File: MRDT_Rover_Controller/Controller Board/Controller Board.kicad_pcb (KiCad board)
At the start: 2 copper layers, 137.6 x 81.5 mm, 29 parts, among them Q1 S8050, U1 MCP3008

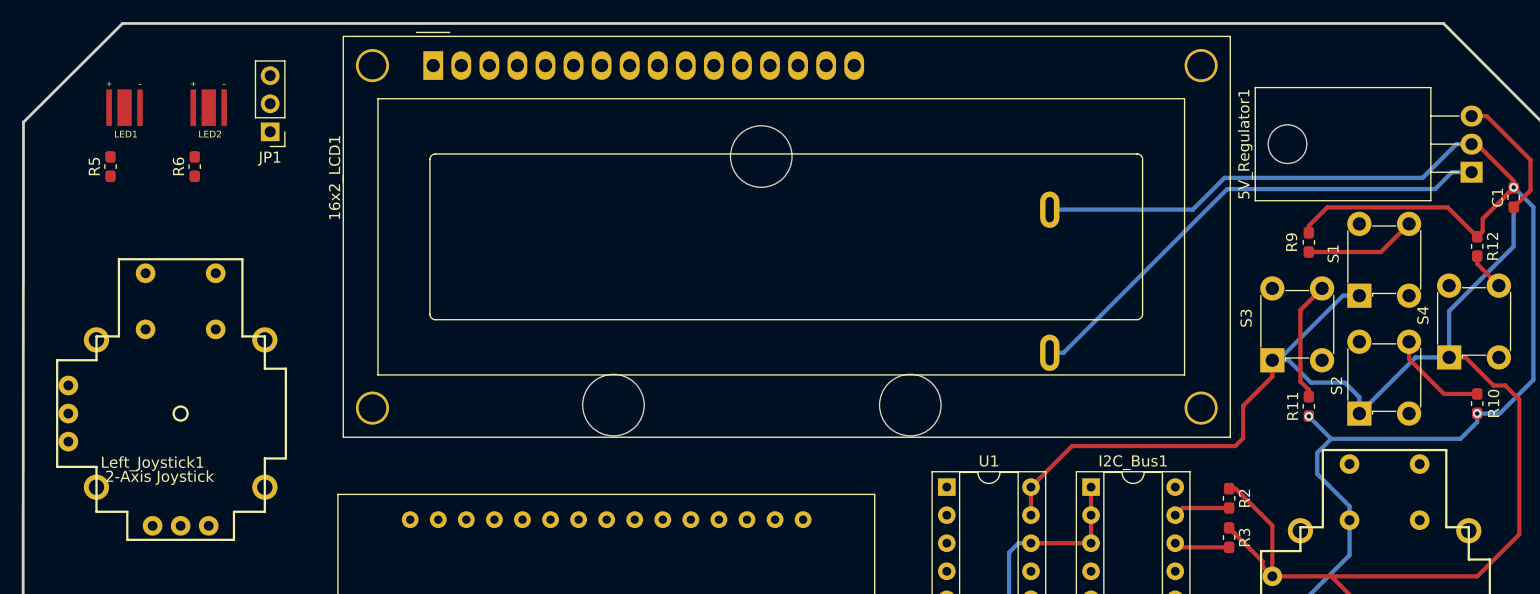
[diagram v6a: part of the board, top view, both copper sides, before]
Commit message: PCB Traces Updated
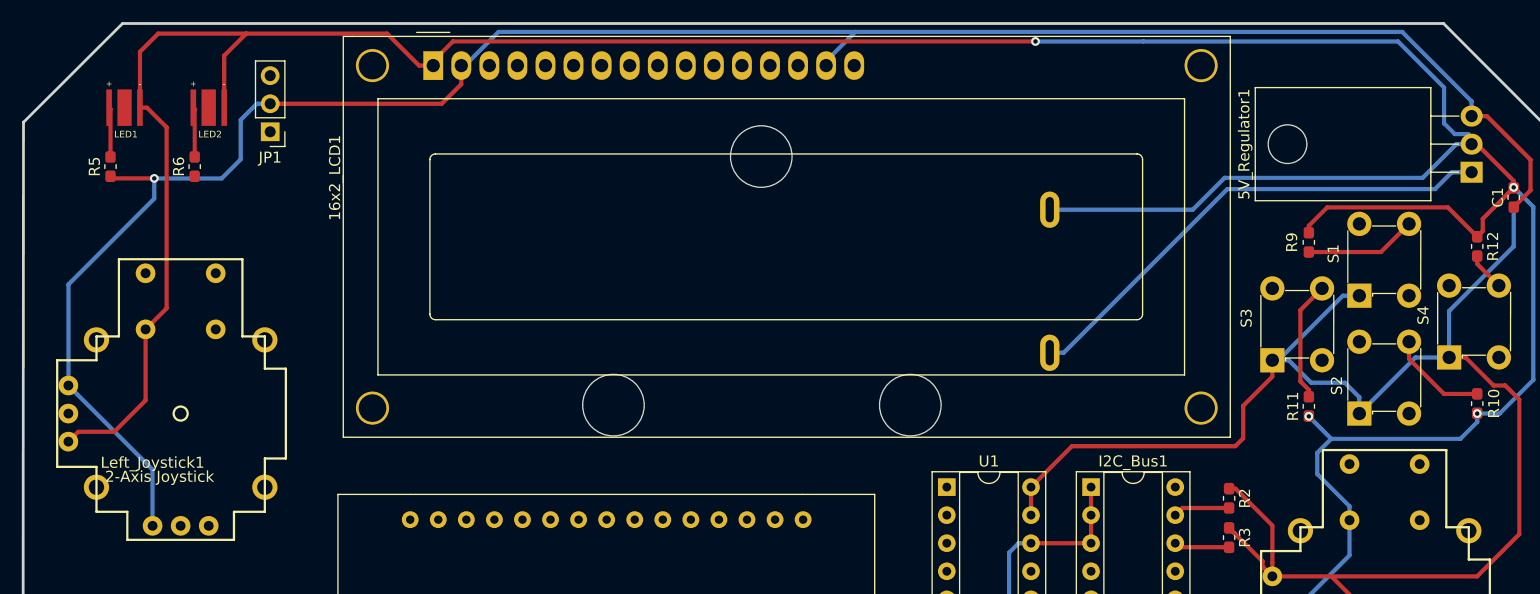
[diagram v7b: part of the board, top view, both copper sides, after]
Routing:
- net GND: track 225.5 -> 404.9 mm, vias 3 -> 4
- net 5V: track 164.4 -> 342.1 mm, vias 0 -> 1
- net Net-(LED2-Pad1): track 0.00 -> 4.51 mm
- net Net-(LED1-Pad1): track 0.00 -> 4.51 mm
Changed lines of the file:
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@@
     (thickness 1.6)
     (drawings 25)
-    (tracks 120)
+    (tracks 179)
     (zones 0)
     (modules 29)
@@
   (segment (start 164.8968 114.046) (end 167.132 111.8108) (width 0.381) (layer F.Cu) (net 14))
   (segment (start 164.8968 118.6434) (end 164.8968 114.046) (width 0.381) (layer F.Cu) (net 14))
+  (segment (start 207.01 62.398802) (end 206.688798 62.0776) (width 0.381) (layer B.Cu) (net 14))
+  (segment (start 207.01 62.992) (end 207.01 62.398802) (width 0.381) (layer B.Cu) (net 14))
+  (segment (start 206.688798 62.0776) (end 205.486 62.0776) (width 0.381) (layer B.Cu) (net 14))
+  (segment (start 204.5208 61.1124) (end 204.5208 57.8612) (width 0.381) (layer B.Cu) (net 14))
+  (segment (start 205.486 62.0776) (end 204.5208 61.1124) (width 0.381) (layer B.Cu) (net 14))
+  (segment (start 204.5208 57.8612) (end 200.3552 53.6956) (width 0.381) (layer B.Cu) (net 14))
+  (segment (start 200.3552 53.6956) (end 177.292 53.6956) (width 0.381) (layer B.Cu) (net 14))
+  (segment (start 177.292 53.6956) (end 167.5384 53.6956) (width 0.381) (layer B.Cu) (net 14))
+  (segment (start 167.5384 53.6956) (end 167.5384 53.6956) (width 0.381) (layer B.Cu) (net 14))
+  (via (at 167.5384 53.6956) (size 0.8) (drill 0.4) (layers F.Cu B.Cu) (net 14))
+  (segment (start 113.03 55.48) (end 113.03 55.88) (width 0.381) (layer F.Cu) (net 14))
+  (segment (start 114.8144 53.6956) (end 113.03 55.48) (width 0.381) (layer F.Cu) (net 14))
+  (segment (start 167.5384 53.6956) (end 114.8144 53.6956) (width 0.381) (layer F.Cu) (net 14))
+  (segment (start 111.749 55.88) (end 108.8534 52.9844) (width 0.381) (layer F.Cu) (net 14))
+  (segment (start 113.03 55.88) (end 111.749 55.88) (width 0.381) (layer F.Cu) (net 14))
+  (segment (start 108.8534 52.9844) (end 96.1136 52.9844) (width 0.381) (layer F.Cu) (net 14))
+  (segment (start 94.107 54.991) (end 94.107 59.69) (width 0.381) (layer F.Cu) (net 14))
+  (segment (start 96.1136 52.9844) (end 94.107 54.991) (width 0.381) (layer F.Cu) (net 14))
+  (segment (start 86.487 59.69) (end 86.487 54.6354) (width 0.381) (layer F.Cu) (net 14))
+  (segment (start 88.138 52.9844) (end 96.1136 52.9844) (width 0.381) (layer F.Cu) (net 14))
+  (segment (start 86.487 54.6354) (end 88.138 52.9844) (width 0.381) (layer F.Cu) (net 14))
+  (segment (start 87.122 59.69) (end 88.9 61.468) (width 0.381) (layer F.Cu) (net 14))
+  (segment (start 86.487 59.69) (end 87.122 59.69) (width 0.381) (layer F.Cu) (net 14))
+  (segment (start 88.9 77.851) (end 86.995 79.756) (width 0.381) (layer F.Cu) (net 14))
+  (segment (start 88.9 61.468) (end 88.9 77.851) (width 0.381) (layer F.Cu) (net 14))
+  (segment (start 80.898999 89.027001) (end 84.150199 89.027001) (width 0.381) (layer F.Cu) (net 14))
+  (segment (start 80.01 89.916) (end 80.898999 89.027001) (width 0.381) (layer F.Cu) (net 14))
+  (segment (start 86.995 86.1822) (end 84.150199 89.027001) (width 0.381) (layer F.Cu) (net 14))
+  (segment (start 86.995 79.756) (end 86.995 86.1822) (width 0.381) (layer F.Cu) (net 14))
   (segment (start 170.086 81.874) (end 184.904 67.056) (width 0.381) (layer B.Cu) (net 15))
   (segment (start 168.83 81.874) (end 170.086 81.874) (width 0.381) (layer B.Cu) (net 15))
@@
   (segment (start 180.5546 99.4778) (end 180.1876 99.1108) (width 0.381) (layer F.Cu) (net 36))
   (segment (start 185.0644 99.4778) (end 180.5546 99.4778) (width 0.381) (layer F.Cu) (net 36))
+  (segment (start 83.82 59.817) (end 83.693 59.69) (width 0.381) (layer F.Cu) (net 43))
+  (segment (start 83.82 64.149) (end 83.82 59.817) (width 0.381) (layer F.Cu) (net 43))
+  (segment (start 91.44 59.817) (end 91.313 59.69) (width 0.381) (layer F.Cu) (net 45))
+  (segment (start 91.44 64.149) (end 91.44 59.817) (width 0.381) (layer F.Cu) (net 45))
   (segment (start 207.518 73.836) (end 209.478 75.796) (width 0.381) (layer F.Cu) (net 54))
   (segment (start 207.518 73.124) (end 207.518 73.836) (width 0.381) (layer F.Cu) (net 54))
@@
   (segment (start 185.6232 90.3224) (end 170.8404 90.3224) (width 0.381) (layer F.Cu) (net 66))
   (segment (start 167.132 94.0308) (end 167.132 96.5708) (width 0.381) (layer F.Cu) (net 66))
+  (segment (start 148.59 55.48) (end 148.59 55.88) (width 0.381) (layer B.Cu) (net 66))
+  (segment (start 151.238 52.832) (end 148.59 55.48) (width 0.381) (layer B.Cu) (net 66))
+  (segment (start 200.7235 52.832) (end 151.238 52.832) (width 0.381) (layer B.Cu) (net 66))
+  (segment (start 207.01 59.1185) (end 200.7235 52.832) (width 0.381) (layer B.Cu) (net 66))
+  (segment (start 207.01 60.452) (end 207.01 59.1185) (width 0.381) (layer B.Cu) (net 66))
+  (segment (start 118.932944 52.832) (end 151.238 52.832) (width 0.381) (layer B.Cu) (net 66))
+  (segment (start 115.884944 55.88) (end 118.932944 52.832) (width 0.381) (layer B.Cu) (net 66))
+  (segment (start 115.57 55.88) (end 115.884944 55.88) (width 0.381) (layer B.Cu) (net 66))
+  (segment (start 99.474681 59.3344) (end 98.2726 59.3344) (width 0.381) (layer F.Cu) (net 66))
+  (segment (start 113.7966 59.3344) (end 99.474681 59.3344) (width 0.381) (layer F.Cu) (net 66))
+  (segment (start 115.57 57.561) (end 113.7966 59.3344) (width 0.381) (layer F.Cu) (net 66))
+  (segment (start 115.57 55.88) (end 115.57 57.561) (width 0.381) (layer F.Cu) (net 66))
+  (segment (start 97.070519 59.3344) (end 95.6056 60.799319) (width 0.381) (layer B.Cu) (net 66))
+  (segment (start 98.2726 59.3344) (end 97.070519 59.3344) (width 0.381) (layer B.Cu) (net 66))
+  (segment (start 95.6056 60.799319) (end 95.6056 64.3636) (width 0.381) (layer B.Cu) (net 66))
+  (segment (start 95.6056 64.3636) (end 93.8784 66.0908) (width 0.381) (layer B.Cu) (net 66))
+  (segment (start 93.8784 66.0908) (end 87.7824 66.0908) (width 0.381) (layer B.Cu) (net 66))
+  (segment (start 87.7824 66.0908) (end 87.7824 66.0908) (width 0.381) (layer B.Cu) (net 66))
+  (via (at 87.7824 66.0908) (size 0.8) (drill 0.4) (layers F.Cu B.Cu) (net 66))
+  (segment (start 84.0118 66.0908) (end 83.82 65.899) (width 0.381) (layer F.Cu) (net 66))
+  (segment (start 87.7824 66.0908) (end 84.0118 66.0908) (width 0.381) (layer F.Cu) (net 66))
+  (segment (start 80.01 84.836) (end 80.01 75.692) (width 0.381) (layer B.Cu) (net 66))
+  (segment (start 87.7824 67.9196) (end 87.7824 66.0908) (width 0.381) (layer B.Cu) (net 66))
+  (segment (start 80.01 75.692) (end 87.7824 67.9196) (width 0.381) (layer B.Cu) (net 66))
+  (segment (start 87.63 92.456) (end 80.01 84.836) (width 0.381) (layer B.Cu) (net 66))
+  (segment (start 87.63 97.536) (end 87.63 92.456) (width 0.381) (layer B.Cu) (net 66))
 )

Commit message: PCB Updated
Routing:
- net SW1: track 10.1 -> 76.7 mm
- net 5V: track 342.1 -> 346.4 mm
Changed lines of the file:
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@@
     (thickness 1.6)
     (drawings 25)
-    (tracks 179)
+    (tracks 194)
     (zones 0)
     (modules 29)
@@
   )
   (setup
-    (last_trace_width 0.381)
+    (last_trace_width 0.25)
     (user_trace_width 0.381)
     (user_trace_width 15)
@@
   (segment (start 198.801 72.757) (end 201.35 70.208) (width 0.381) (layer F.Cu) (net 57))
   (segment (start 192.278 72.757) (end 198.801 72.757) (width 0.381) (layer F.Cu) (net 57))
+  (segment (start 192.278 72.757) (end 189.8282 72.757) (width 0.25) (layer F.Cu) (net 57))
+  (segment (start 189.8282 72.757) (end 179.7304 82.8548) (width 0.25) (layer F.Cu) (net 57))
+  (segment (start 179.7304 82.8548) (end 179.7304 88.2396) (width 0.25) (layer F.Cu) (net 57))
+  (segment (start 179.7304 88.2396) (end 178.562 89.408) (width 0.25) (layer F.Cu) (net 57))
+  (segment (start 178.562 89.408) (end 170.5356 89.408) (width 0.25) (layer F.Cu) (net 57))
+  (segment (start 170.5356 89.408) (end 168.0464 91.8972) (width 0.25) (layer F.Cu) (net 57))
+  (segment (start 139.649199 96.215201) (end 138.8872 96.9772) (width 0.25) (layer F.Cu) (net 57))
+  (segment (start 139.974201 95.890199) (end 139.649199 96.215201) (width 0.25) (layer F.Cu) (net 57))
+  (segment (start 141.193401 95.890199) (end 139.974201 95.890199) (width 0.25) (layer F.Cu) (net 57))
+  (segment (start 145.1864 91.8972) (end 141.193401 95.890199) (width 0.25) (layer F.Cu) (net 57))
+  (segment (start 168.0464 91.8972) (end 145.1864 91.8972) (width 0.25) (layer F.Cu) (net 57))
   (segment (start 208.391 60.452) (end 212.344 64.405) (width 0.381) (layer F.Cu) (net 66))
   (segment (start 207.01 60.452) (end 208.391 60.452) (width 0.381) (layer F.Cu) (net 66))
@@
   (segment (start 186.3344 89.6112) (end 185.6232 90.3224) (width 0.381) (layer F.Cu) (net 66))
   (segment (start 170.8404 90.3224) (end 167.132 94.0308) (width 0.381) (layer F.Cu) (net 66))
-  (segment (start 185.6232 90.3224) (end 170.8404 90.3224) (width 0.381) (layer F.Cu) (net 66))
   (segment (start 167.132 94.0308) (end 167.132 96.5708) (width 0.381) (layer F.Cu) (net 66))
   (segment (start 148.59 55.48) (end 148.59 55.88) (width 0.381) (layer B.Cu) (net 66))
@@
   (segment (start 87.63 92.456) (end 80.01 84.836) (width 0.381) (layer B.Cu) (net 66))
   (segment (start 87.63 97.536) (end 87.63 92.456) (width 0.381) (layer B.Cu) (net 66))
+  (segment (start 180.987599 90.843201) (end 181.5084 90.3224) (width 0.25) (layer F.Cu) (net 66))
+  (segment (start 180.987599 93.230801) (end 180.987599 90.843201) (width 0.25) (layer F.Cu) (net 66))
+  (segment (start 180.1876 94.0308) (end 180.987599 93.230801) (width 0.25) (layer F.Cu) (net 66))
+  (segment (start 185.6232 90.3224) (end 181.5084 90.3224) (width 0.381) (layer F.Cu) (net 66))
+  (segment (start 181.5084 90.3224) (end 170.8404 90.3224) (width 0.381) (layer F.Cu) (net 66))
 )
